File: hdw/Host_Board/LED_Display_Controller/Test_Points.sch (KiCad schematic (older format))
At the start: 7 parts

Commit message: Removed 15 of the 20 original outptu power connectors, added a few test points
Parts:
- added TP? (x3): TP, symbol Custom_Library:TP
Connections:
- net labels added: +3.3V, +5.5V_MNG, +5V
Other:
- moved on the sheet: TP?
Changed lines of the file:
@@
 $Descr A 11000 8500
 encoding utf-8
-Sheet 26 31
+Sheet 26 32
 Title ""
 Date ""
@@
 L LED_Display_Local_Library:GND_USB #PWR?
 U 1 1 5BBFA77B
-P 3000 6040
+P 4680 6050
 AR Path="/5BAAE1F3/5BBFA77B" Ref="#PWR?"  Part="1"
 AR Path="/5BBF5233/5BBFA77B" Ref="#PWR?"  Part="1"
-F 0 "#PWR?" H 3000 5790 50  0001 C CNN
-F 1 "GND_USB" H 3000 5890 50  0000 C CNN
-F 2 "" H 3000 6040 50  0001 C CNN
-F 3 "" H 3000 6040 50  0001 C CNN
-	1    3000 6040
+F 0 "#PWR?" H 4680 5800 50  0001 C CNN
+F 1 "GND_USB" H 4680 5900 50  0000 C CNN
+F 2 "" H 4680 6050 50  0001 C CNN
+F 3 "" H 4680 6050 50  0001 C CNN
+	1    4680 6050
 	1    0    0    -1
 $EndComp
@@
 L Connector:TestPoint TP?
 U 1 1 5BBFA781
-P 3000 6040
+P 4680 6050
 AR Path="/5BAAE1F3/5BBFA781" Ref="TP?"  Part="1"
 AR Path="/5BBF5233/5BBFA781" Ref="TP?"  Part="1"
-F 0 "TP?" H 3000 6250 50  0000 C CNN
-F 1 "TestPoint" H 3000 6240 50  0001 C CNN
-F 2 "" H 3200 6040 50  0001 C CNN
-F 3 "~" H 3200 6040 50  0001 C CNN
-	1    3000 6040
+F 0 "TP?" H 4680 6260 50  0000 C CNN
+F 1 "TestPoint" H 4680 6250 50  0001 C CNN
+F 2 "" H 4880 6050 50  0001 C CNN
+F 3 "~" H 4880 6050 50  0001 C CNN
+	1    4680 6050
 	1    0    0    -1
 $EndComp
@@
 L Custom_Library:TP TP?
 U 1 1 5BBFB09C
-P 3650 6000
-F 0 "TP?" H 3650 6150 50  0000 C CNN
-F 1 "TP" H 3650 6150 50  0001 C CNN
-F 2 "" H 3650 6000 60  0000 C CNN
-F 3 "" H 3650 6000 60  0000 C CNN
-	1    3650 6000
+P 5330 6010
+F 0 "TP?" H 5330 6160 50  0000 C CNN
+F 1 "TP" H 5330 6160 50  0001 C CNN
+F 2 "" H 5330 6010 60  0000 C CNN
+F 3 "" H 5330 6010 60  0000 C CNN
+	1    5330 6010
 	1    0    0    -1
 $EndComp
@@
 L Custom_Library:+5V_USB #PWR?
 U 1 1 5BBFB102
-P 3650 6000
-F 0 "#PWR?" H 3650 5850 50  0001 C CNN
-F 1 "+5V_USB" H 3650 6140 50  0000 C CNN
-F 2 "" H 3650 6000 50  0001 C CNN
-F 3 "" H 3650 6000 50  0001 C CNN
-	1    3650 6000
+P 5330 6010
+F 0 "#PWR?" H 5330 5860 50  0001 C CNN
+F 1 "+5V_USB" H 5330 6150 50  0000 C CNN
+F 2 "" H 5330 6010 50  0001 C CNN
+F 3 "" H 5330 6010 50  0001 C CNN
+	1    5330 6010
 	-1   0    0    1
 $EndComp
@@
 Wire Wire Line
 	9420 2960 9340 2960
+$Comp
+L Custom_Library:TP TP?
+U 1 1 5BD1E3B2
+P 2940 5980
+AR Path="/5BAAE0FA/5BD1E3B2" Ref="TP?"  Part="1"
+AR Path="/5BBF5233/5BD1E3B2" Ref="TP?"  Part="1"
+F 0 "TP?" H 2940 6130 50  0000 C CNN
+F 1 "TP" H 2940 6130 50  0001 C CNN
+F 2 "" H 2940 5980 60  0000 C CNN
+F 3 "" H 2940 5980 60  0000 C CNN
+	1    2940 5980
+	-1   0    0    1
+$EndComp
+$Comp
+L power:+3.3V #PWR?
+U 1 1 5BD1E45C
+P 2940 5980
+F 0 "#PWR?" H 2940 5830 50  0001 C CNN
+F 1 "+3.3V" H 2940 6120 50  0000 C CNN
+F 2 "" H 2940 5980 50  0001 C CNN
+F 3 "" H 2940 5980 50  0001 C CNN
+	1    2940 5980
+	1    0    0    -1
+$EndComp
+$Comp
+L Custom_Library:TP TP?
+U 1 1 5BD1E47E
+P 3330 5980
+AR Path="/5BAAE0FA/5BD1E47E" Ref="TP?"  Part="1"
+AR Path="/5BBF5233/5BD1E47E" Ref="TP?"  Part="1"
+F 0 "TP?" H 3330 6130 50  0000 C CNN
+F 1 "TP" H 3330 6130 50  0001 C CNN
+F 2 "" H 3330 5980 60  0000 C CNN
+F 3 "" H 3330 5980 60  0000 C CNN
+	1    3330 5980
+	-1   0    0    1
+$EndComp
+$Comp
+L power:+5V #PWR?
+U 1 1 5BD1E4E3
+P 3330 5980
+F 0 "#PWR?" H 3330 5830 50  0001 C CNN
+F 1 "+5V" H 3330 6120 50  0000 C CNN
+F 2 "" H 3330 5980 50  0001 C CNN
+F 3 "" H 3330 5980 50  0001 C CNN
+	1    3330 5980
+	1    0    0    -1
+$EndComp
+$Comp
+L Custom_Library:TP TP?
+U 1 1 5BD1E507
+P 3790 5980
+AR Path="/5BAAE0FA/5BD1E507" Ref="TP?"  Part="1"
+AR Path="/5BBF5233/5BD1E507" Ref="TP?"  Part="1"
+F 0 "TP?" H 3790 6130 50  0000 C CNN
+F 1 "TP" H 3790 6130 50  0001 C CNN
+F 2 "" H 3790 5980 60  0000 C CNN
+F 3 "" H 3790 5980 60  0000 C CNN
+	1    3790 5980
+	-1   0    0    1
+$EndComp
+$Comp
+L Custom_Library:+5.5V_MNG #PWR?
+U 1 1 5BD1E578
+P 3790 5980
+F 0 "#PWR?" H 3790 5830 50  0001 C CNN
+F 1 "+5.5V_MNG" H 3790 6120 50  0000 C CNN
+F 2 "" H 3790 5980 50  0001 C CNN
+F 3 "" H 3790 5980 50  0001 C CNN
+	1    3790 5980
+	1    0    0    -1
+$EndComp
 $EndSCHEMATC

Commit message: Added a few pages for more features
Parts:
- removed TP? (x2): TP, symbol Custom_Library:TP
- added J?: WIFI UART, symbol Connector_Generic:Conn_01x03
- J?: value UART -> USB UART
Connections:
- net labels added: WIFI_UART_RX, WIFI_UART_TX
- net labels removed: +5.5V_MNG, +5V
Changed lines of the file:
@@
 $Descr A 11000 8500
 encoding utf-8
-Sheet 26 25
+Sheet 25 30
 Title ""
 Date ""
@@
 AR Path="/5BAAE1DC/5BBF638E" Ref="J?"  Part="1"
 AR Path="/5BBF5233/5BBF638E" Ref="J?"  Part="1"
-F 0 "J?" H 1980 1350 50  0000 C CNN
-F 1 "UART" H 1980 950 50  0000 C CNN
+F 0 "J?" H 2060 1192 50  0000 L CNN
+F 1 "USB UART" H 2060 1101 50  0000 L CNN
 F 2 "" H 1980 1150 50  0001 C CNN
 F 3 "~" H 1980 1150 50  0001 C CNN
@@
 	1    0    0    -1
 $EndComp
-$Comp
-L Custom_Library:TP TP?
-U 1 1 5BD1E47E
-P 3330 5980
-AR Path="/5BAAE0FA/5BD1E47E" Ref="TP?"  Part="1"
-AR Path="/5BBF5233/5BD1E47E" Ref="TP?"  Part="1"
-F 0 "TP?" H 3330 6130 50  0000 C CNN
-F 1 "TP" H 3330 6130 50  0001 C CNN
-F 2 "" H 3330 5980 60  0000 C CNN
-F 3 "" H 3330 5980 60  0000 C CNN
-	1    3330 5980
-	-1   0    0    1
-$EndComp
-$Comp
-L power:+5V #PWR?
-U 1 1 5BD1E4E3
-P 3330 5980
-F 0 "#PWR?" H 3330 5830 50  0001 C CNN
-F 1 "+5V" H 3330 6120 50  0000 C CNN
-F 2 "" H 3330 5980 50  0001 C CNN
-F 3 "" H 3330 5980 50  0001 C CNN
-	1    3330 5980
-	1    0    0    -1
-$EndComp
-$Comp
-L Custom_Library:TP TP?
-U 1 1 5BD1E507
-P 3790 5980
-AR Path="/5BAAE0FA/5BD1E507" Ref="TP?"  Part="1"
-AR Path="/5BBF5233/5BD1E507" Ref="TP?"  Part="1"
-F 0 "TP?" H 3790 6130 50  0000 C CNN
-F 1 "TP" H 3790 6130 50  0001 C CNN
-F 2 "" H 3790 5980 60  0000 C CNN
-F 3 "" H 3790 5980 60  0000 C CNN
-	1    3790 5980
-	-1   0    0    1
-$EndComp
-$Comp
-L Custom_Library:+5.5V_MNG #PWR?
-U 1 1 5BD1E578
-P 3790 5980
-F 0 "#PWR?" H 3790 5830 50  0001 C CNN
-F 1 "+5.5V_MNG" H 3790 6120 50  0000 C CNN
-F 2 "" H 3790 5980 50  0001 C CNN
-F 3 "" H 3790 5980 50  0001 C CNN
-	1    3790 5980
-	1    0    0    -1
-$EndComp
+Text GLabel 3420 1050 0    50   UnSpc ~ 0
+WIFI_UART_TX
+Text GLabel 3420 1150 0    50   UnSpc ~ 0
+WIFI_UART_RX
+$Comp
+L Connector_Generic:Conn_01x03 J?
+U 1 1 5BE765ED
+P 3620 1150
+AR Path="/5BAAE1DC/5BE765ED" Ref="J?"  Part="1"
+AR Path="/5BBF5233/5BE765ED" Ref="J?"  Part="1"
+F 0 "J?" H 3700 1192 50  0000 L CNN
+F 1 "WIFI UART" H 3700 1101 50  0000 L CNN
+F 2 "" H 3620 1150 50  0001 C CNN
+F 3 "~" H 3620 1150 50  0001 C CNN
+	1    3620 1150
+	1    0    0    -1
+$EndComp
+$Comp
+L power:GND #PWR?
+U 1 1 5BE765F6
+P 3420 1250
+AR Path="/5BAAE1DC/5BE765F6" Ref="#PWR?"  Part="1"
+AR Path="/5BBF5233/5BE765F6" Ref="#PWR?"  Part="1"
+F 0 "#PWR?" H 3420 1000 50  0001 C CNN
+F 1 "GND" H 3420 1100 50  0000 C CNN
+F 2 "" H 3420 1250 50  0001 C CNN
+F 3 "" H 3420 1250 50  0001 C CNN
+	1    3420 1250
+	1    0    0    -1
+$EndComp

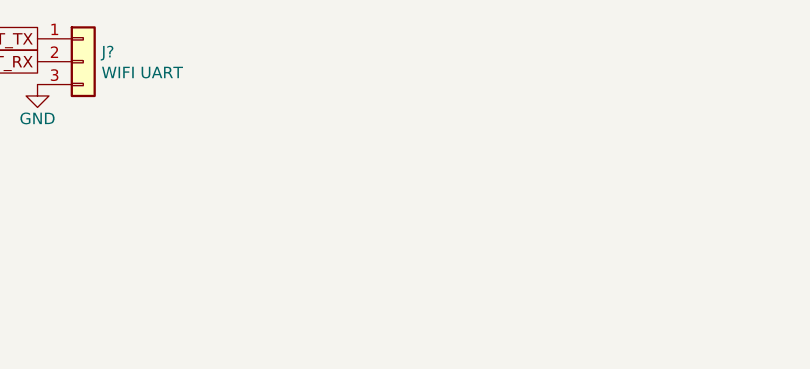
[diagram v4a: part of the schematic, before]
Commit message: Added panel output enable AND gate
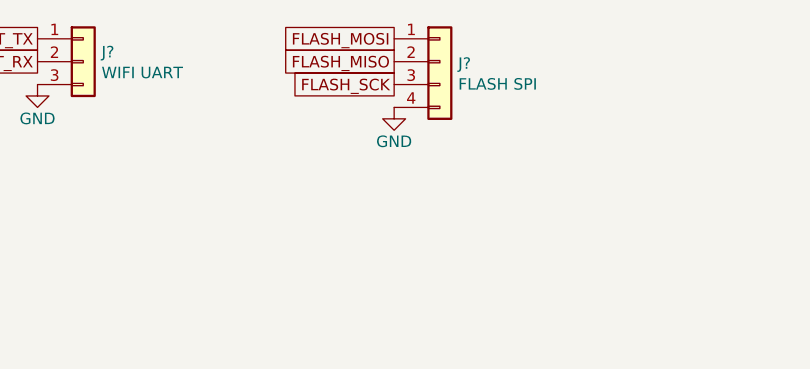
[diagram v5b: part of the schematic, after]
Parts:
- added J?: FLASH SPI, symbol Connector_Generic:Conn_01x04
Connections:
- net GND: now also J?.4 (Pin_4)
- new net FLASH_MISO: J?.2 (Pin_2)
- new net FLASH_MOSI: J?.1 (Pin_1)
- new net FLASH_SCK: J?.3 (Pin_3)
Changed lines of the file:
@@
 	1    0    0    -1
 $EndComp
+$Comp
+L Connector_Generic:Conn_01x04 J?
+U 1 1 5BF544D4
+P 5180 1150
+F 0 "J?" H 5260 1142 50  0000 L CNN
+F 1 "FLASH SPI" H 5260 1051 50  0000 L CNN
+F 2 "" H 5180 1150 50  0001 C CNN
+F 3 "~" H 5180 1150 50  0001 C CNN
+	1    5180 1150
+	1    0    0    -1
+$EndComp
+$Comp
+L power:GND #PWR?
+U 1 1 5BF54513
+P 4980 1350
+AR Path="/5BAAE1DC/5BF54513" Ref="#PWR?"  Part="1"
+AR Path="/5BBF5233/5BF54513" Ref="#PWR?"  Part="1"
+F 0 "#PWR?" H 4980 1100 50  0001 C CNN
+F 1 "GND" H 4980 1200 50  0000 C CNN
+F 2 "" H 4980 1350 50  0001 C CNN
+F 3 "" H 4980 1350 50  0001 C CNN
+	1    4980 1350
+	1    0    0    -1
+$EndComp
+Text GLabel 4980 1250 0    50   UnSpc ~ 0
+FLASH_SCK
+Text GLabel 4980 1050 0    50   UnSpc ~ 0
+FLASH_MOSI
+Text GLabel 4980 1150 0    50   UnSpc ~ 0
+FLASH_MISO
 $EndSCHEMATC

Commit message: rage commit
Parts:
- added TP? (x2): TP, symbol Custom_Library:TP
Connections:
- new net +5.5V: TP?.1 (TP)
- new net +5V: TP?.1 (TP)
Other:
- note added: "30. Test Points"
- moved on the sheet: J?
